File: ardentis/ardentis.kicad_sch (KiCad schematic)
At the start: 0 parts

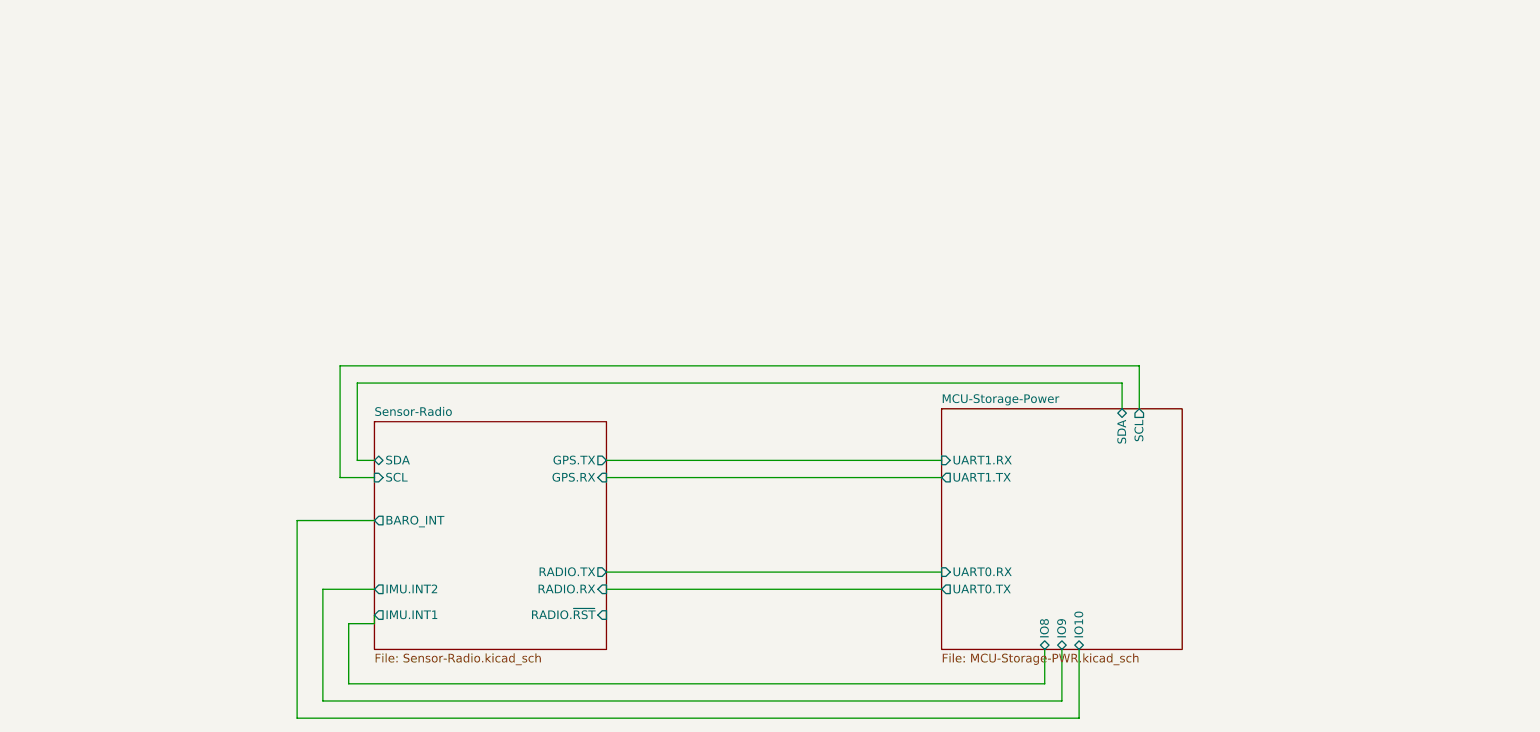
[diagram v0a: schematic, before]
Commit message: Initial code
Initial code. Theoretically will work but not tested due to lack of hardware and updates to PCB.
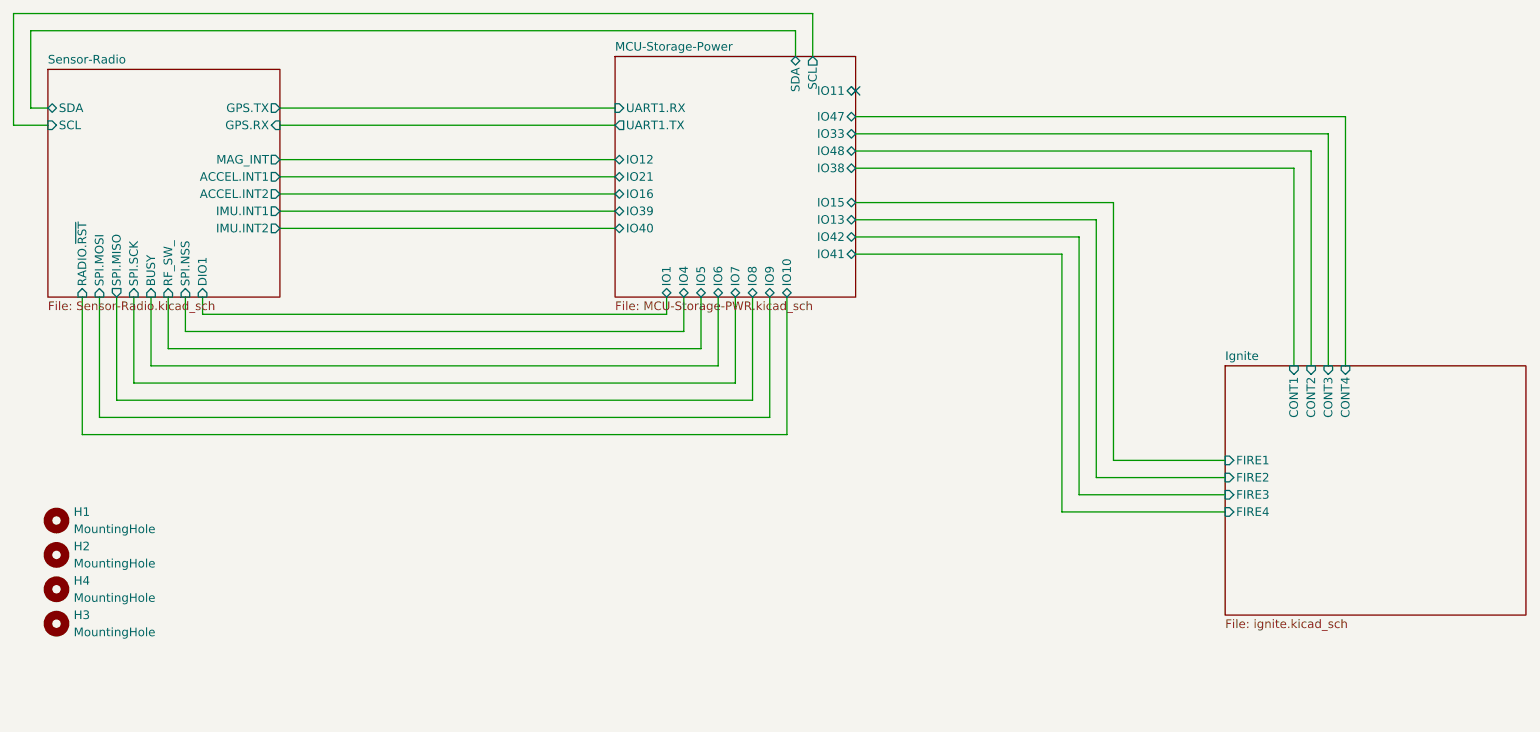
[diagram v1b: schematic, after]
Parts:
- added H1, H2, H3, H4: MountingHole, Library:MountingHole_3.5mm_Pad, symbol Library:MountingHole
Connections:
- no-connect marks 0 -> 1
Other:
- added sheet Ignite (ignite.kicad_sch)
- sheet MCU-Storage-Power ports: added IO1, IO11, IO12, IO13, IO15, IO16, IO21, IO33, IO38, IO39, IO4, IO40, IO41, IO42, IO47, IO48, IO5, IO6, IO7; removed UART0.RX, UART0.TX
- sheet Sensor-Radio ports: added ACCEL.INT1, ACCEL.INT2, BUSY, DIO1, MAG_INT, RF_SW_, SPI.MISO, SPI.MOSI, SPI.NSS, SPI.SCK; removed BARO_INT, RADIO.RX, RADIO.TX
- company: (none) -> CU INSPACE
